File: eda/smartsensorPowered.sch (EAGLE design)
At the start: 39 parts, among them Q1 IRFML8244, Q2 IRFML8244, Q3 IRFML8244, Q4 IRFML8244

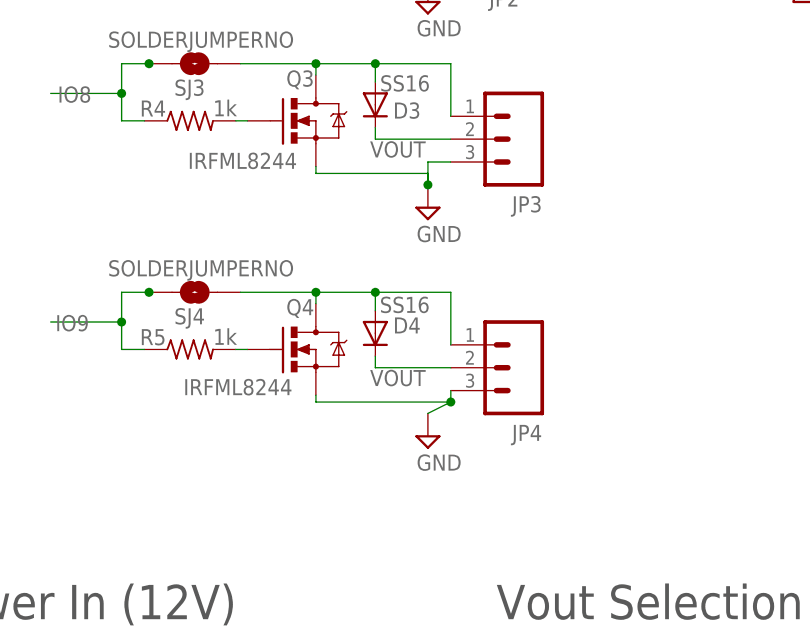
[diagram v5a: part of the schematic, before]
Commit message: Fix for smartsensorPowered brd and sch #3 - aligned the JP connectors properly - Changed Rev from Rev. C to Rev. B
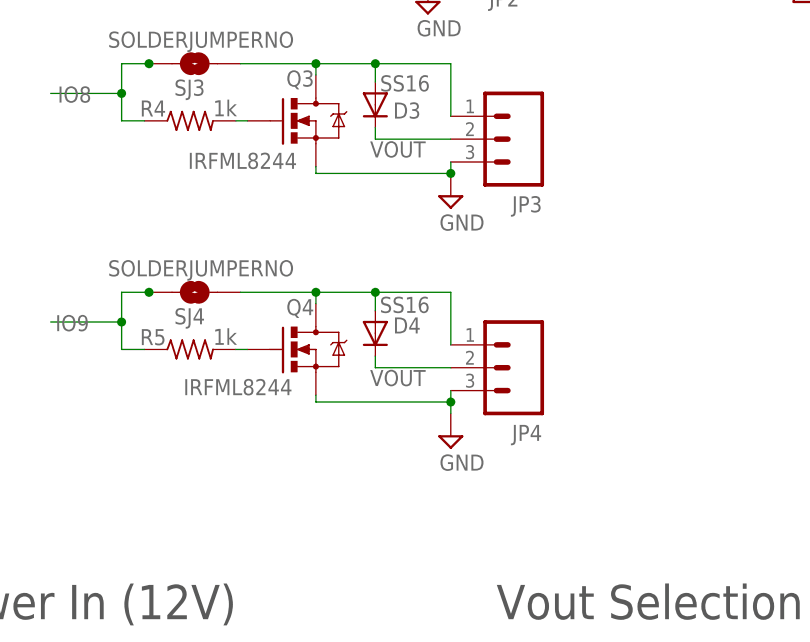
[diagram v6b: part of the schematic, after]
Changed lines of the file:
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@@
 <part name="FRAME1" library="pie" deviceset="FRAME-LETTER" device="">
 <attribute name="AUTHOR" value="Vincent D, Devin H, Kate R, Andrew H, Sumita G, Tobin H, Casey D."/>
-<attribute name="REVISION" value="4C"/>
+<attribute name="REVISION" value="4B"/>
 </part>
 <part name="SUPPLY10" library="pie" deviceset="GND" device=""/>
@@
 <attribute name="VALUE" x="54.864" y="119.38" size="1.778" layer="96" font="vector"/>
 </instance>
-<instance part="SUPPLY8" gate="GND" x="78.74" y="86.36"/>
+<instance part="SUPPLY8" gate="GND" x="81.28" y="87.63"/>
 <instance part="Q3" gate="G$1" x="66.294" y="96.012" smashed="yes">
 <attribute name="NAME" x="62.992" y="99.822" size="1.778" layer="95" font="vector"/>
@@
 <attribute name="VALUE" x="54.864" y="96.52" size="1.778" layer="96" font="vector"/>
 </instance>
-<instance part="SUPPLY9" gate="GND" x="78.74" y="60.96"/>
+<instance part="SUPPLY9" gate="GND" x="81.28" y="60.96"/>
 <instance part="Q4" gate="G$1" x="66.294" y="70.612" smashed="yes">
 <attribute name="NAME" x="62.992" y="74.422" size="1.778" layer="95" font="vector"/>
@@
 <pinref part="SUPPLY8" gate="GND" pin="GND"/>
 <pinref part="Q3" gate="G$1" pin="S"/>
-<wire x1="78.74" y1="90.17" x2="78.74" y2="88.9" width="0.1524" layer="91"/>
 <wire x1="66.294" y1="90.932" x2="66.294" y2="90.17" width="0.1524" layer="91"/>
-<wire x1="66.294" y1="90.17" x2="78.74" y2="90.17" width="0.1524" layer="91"/>
-<wire x1="81.28" y1="91.44" x2="78.74" y2="91.44" width="0.1524" layer="91"/>
-<wire x1="78.74" y1="91.44" x2="78.74" y2="88.9" width="0.1524" layer="91"/>
-<junction x="78.74" y="88.9"/>
+<wire x1="66.294" y1="90.17" x2="81.28" y2="90.17" width="0.1524" layer="91"/>
+<wire x1="81.28" y1="91.44" x2="81.28" y2="90.17" width="0.1524" layer="91"/>
+<junction x="81.28" y="90.17"/>
 </segment>
 <segment>
@@
 <wire x1="81.28" y1="66.04" x2="81.28" y2="64.77" width="0.1524" layer="91"/>
 <pinref part="Q4" gate="G$1" pin="S"/>
-<wire x1="81.28" y1="64.77" x2="78.74" y2="63.5" width="0.1524" layer="91"/>
+<wire x1="81.28" y1="64.77" x2="81.28" y2="63.5" width="0.1524" layer="91"/>
 <wire x1="66.294" y1="65.532" x2="66.294" y2="64.77" width="0.1524" layer="91"/>
 <wire x1="66.294" y1="64.77" x2="81.28" y2="64.77" width="0.1524" layer="91"/>
